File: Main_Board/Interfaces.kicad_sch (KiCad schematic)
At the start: 0 parts

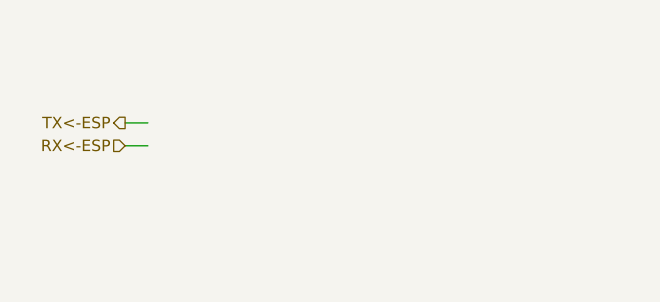
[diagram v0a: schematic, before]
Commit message: RS485 Transciever + Input Protection fix
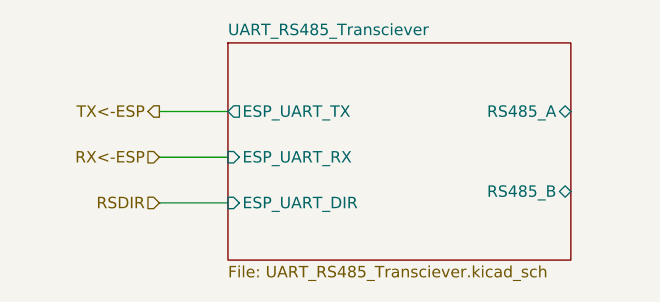
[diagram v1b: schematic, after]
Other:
- added sheet UART_RS485_Transciever (UART_RS485_Transciever.kicad_sch)
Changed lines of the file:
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@@
 	(wire
 		(pts
-			(xy 69.85 92.71) (xy 72.39 92.71)
+			(xy 73.66 91.44) (xy 81.28 91.44)
 		)
 		(stroke
@@
 	(wire
 		(pts
-			(xy 69.85 95.25) (xy 72.39 95.25)
+			(xy 73.66 101.6) (xy 81.28 101.6)
+		)
+		(stroke
+			(width 0)
+			(type default)
+		)
+	)
+	(wire
+		(pts
+			(xy 73.66 96.52) (xy 81.28 96.52)
 		)
 		(stroke
@@
 	(hierarchical_label "RX<-ESP"
 		(shape input)
-		(at 69.85 95.25 180)
+		(at 73.66 96.52 180)
+		(effects
+			(font
+				(size 1.27 1.27)
+			)
+			(justify right)
+		)
+	)
+	(hierarchical_label "RSDIR"
+		(shape input)
+		(at 73.66 101.6 180)
 		(effects
 			(font
@@
 	(hierarchical_label "TX<-ESP"
 		(shape output)
-		(at 69.85 92.71 180)
+		(at 73.66 91.44 180)
 		(effects
 			(font
@@
 		)
 	)
+	(sheet
+		(at 81.28 83.82)
+		(size 38.1 24.13)
+		(exclude_from_sim no)
+		(in_bom yes)
+		(on_board yes)
+		(dnp no)
+		(fields_autoplaced yes)
+		(stroke
+			(width 0.1524)
+			(type solid)
+		)
+		(fill
+			(color 0 0 0 0)
+		)
+		(property "Sheetname" "UART_RS485_Transciever"
+			(at 81.28 83.1084 0)
+			(show_name no)
+			(do_not_autoplace no)
+			(effects
+				(font
+					(size 1.27 1.27)
+				)
+				(justify left bottom)
+			)
+		)
+		(property "Sheetfile" "UART_RS485_Transciever.kicad_sch"
+			(at 81.28 108.5346 0)
+			(show_name no)
+			(do_not_autoplace no)
+			(effects
+				(font
+					(size 1.27 1.27)
+				)
+				(justify left top)
+			)
+		)
+		(pin "ESP_UART_DIR" input
+			(at 81.28 101.6 180)
+			(effects
+				(font
+					(size 1.27 1.27)
+				)
+				(justify left)
+			)
+		)
+		(pin "RS485_B" bidirectional
+			(at 119.38 100.33 0)
+			(effects
+				(font
+					(size 1.27 1.27)
+				)
+				(justify right)
+			)
+		)
+		(pin "ESP_UART_RX" input
+			(at 81.28 96.52 180)
+			(effects
+				(font
+					(size 1.27 1.27)
+				)
+				(justify left)
+			)
+		)
+		(pin "ESP_UART_TX" output
+			(at 81.28 91.44 180)
+			(effects
+				(font
+					(size 1.27 1.27)
+				)
+				(justify left)
+			)
+		)
+		(pin "RS485_A" bidirectional
+			(at 119.38 91.44 0)
+			(effects
+				(font
+					(size 1.27 1.27)
+				)
+				(justify right)
+			)
+		)
+		(instances
+			(project "Main_Board"
+				(path "/7481738f-7c20-40bb-99b0-6ccd4168db33/f339aa79-d1b1-4b60-b951-815db04e9281"
+					(page "9")
+				)
+			)
+		)
+	)

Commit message: Aesthetics/cleanup
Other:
- sheet UART_RS485_Transciever ports: added TRANSCIEVER_UART_DIR, TRANSCIEVER_UART_RX, TRANSCIEVER_UART_TX; removed ESP_UART_DIR, ESP_UART_RX, ESP_UART_TX
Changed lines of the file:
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@@
 	(wire
 		(pts
-			(xy 73.66 91.44) (xy 81.28 91.44)
+			(xy 73.66 101.6) (xy 81.28 101.6)
 		)
 		(stroke
@@
 	(wire
 		(pts
-			(xy 73.66 101.6) (xy 81.28 101.6)
+			(xy 73.66 91.44) (xy 81.28 91.44)
 		)
 		(stroke
@@
 		)
 	)
-	(hierarchical_label "RX<-ESP"
+	(hierarchical_label "MODULE_BUS_RX"
 		(shape input)
 		(at 73.66 96.52 180)
@@
 		)
 	)
-	(hierarchical_label "RSDIR"
+	(hierarchical_label "MODULE_BUS_DIR"
 		(shape input)
 		(at 73.66 101.6 180)
@@
 		)
 	)
-	(hierarchical_label "TX<-ESP"
+	(hierarchical_label "MODULE_BUS_TX"
 		(shape output)
 		(at 73.66 91.44 180)
@@
 			)
 		)
-		(pin "ESP_UART_DIR" input
-			(at 81.28 101.6 180)
-			(effects
-				(font
-					(size 1.27 1.27)
-				)
-				(justify left)
-			)
-		)
 		(pin "RS485_B" bidirectional
 			(at 119.38 100.33 0)
@@
 				)
 				(justify right)
-			)
-		)
-		(pin "ESP_UART_RX" input
-			(at 81.28 96.52 180)
-			(effects
-				(font
-					(size 1.27 1.27)
-				)
-				(justify left)
-			)
-		)
-		(pin "ESP_UART_TX" output
-			(at 81.28 91.44 180)
-			(effects
-				(font
-					(size 1.27 1.27)
-				)
-				(justify left)
 			)
 		)
@@
 			)
 		)
+		(pin "TRANSCIEVER_UART_DIR" input
+			(at 81.28 101.6 180)
+			(effects
+				(font
+					(size 1.27 1.27)
+				)
+				(justify left)
+			)
+		)
+		(pin "TRANSCIEVER_UART_RX" output
+			(at 81.28 96.52 180)
+			(effects
+				(font
+					(size 1.27 1.27)
+				)
+				(justify left)
+			)
+		)
+		(pin "TRANSCIEVER_UART_TX" input
+			(at 81.28 91.44 180)
+			(effects
+				(font
+					(size 1.27 1.27)
+				)
+				(justify left)
+			)
+		)

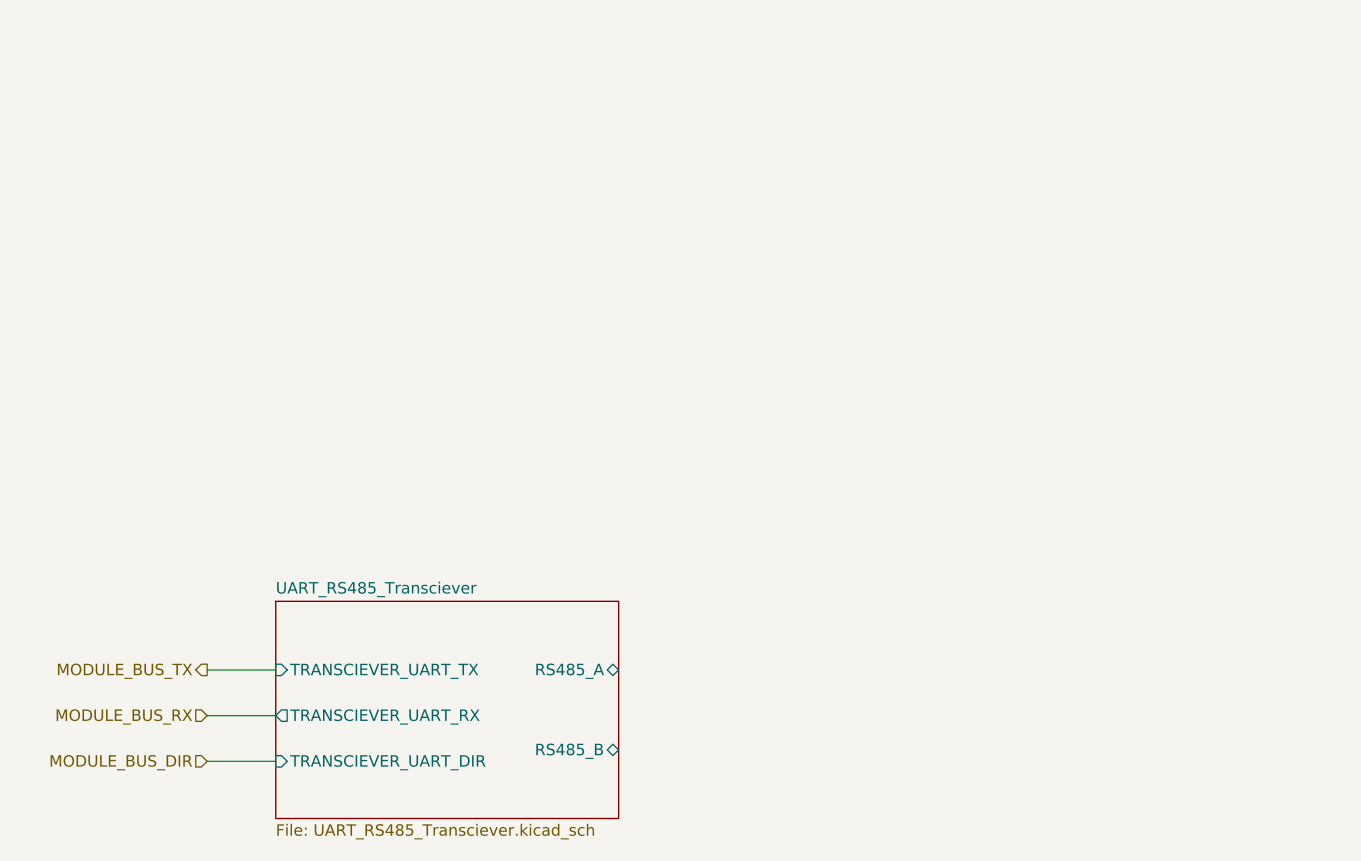
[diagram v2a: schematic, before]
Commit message: add external obrds interfaces
Todo pyro chanells
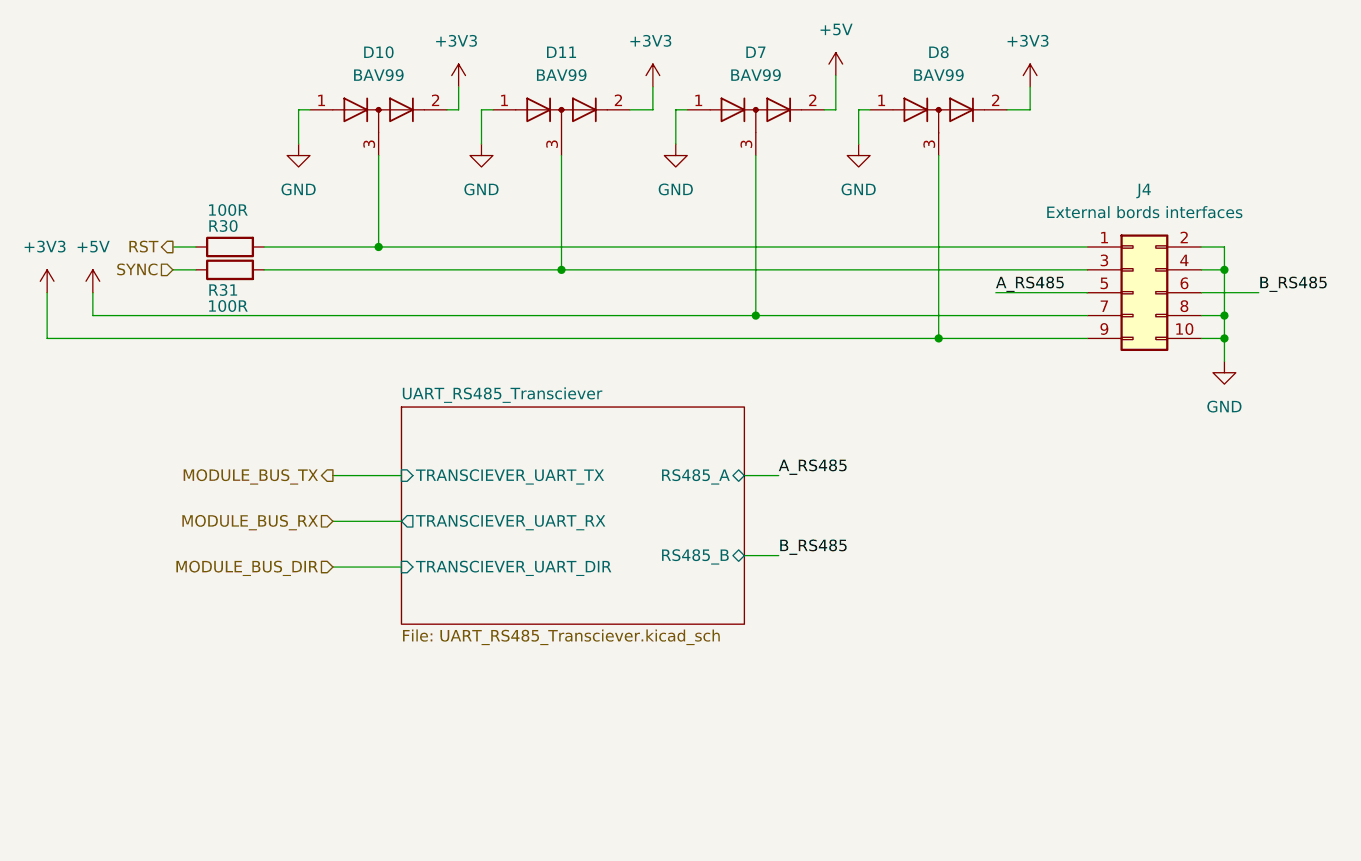
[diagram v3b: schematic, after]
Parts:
- added D10, D11, D7, D8: BAV99, Package_TO_SOT_SMD:SOT-23, symbol Diode:BAV99
- added J4: External bords interfaces, symbol Connector_Generic:Conn_02x05_Odd_Even
- added R30, R31: 100R, symbol Device:R
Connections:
- new net: D10.3 (K), J4.1 (Pin_1), R30.2
- new net: D11.3 (K), J4.3 (Pin_3), R31.2
- new net +3V3: D10.2 (A), D11.2 (A), D8.2 (A), D8.3 (K), J4.9 (Pin_9)
- new net +5V: D7.2 (A), D7.3 (K), J4.7 (Pin_7)
- new net A_RS485: J4.5 (Pin_5)
- new net B_RS485: J4.6 (Pin_6)
- new net GND: D10.1 (K), D11.1 (K), D7.1 (K), D8.1 (K), J4.10 (Pin_10), J4.2 (Pin_2), J4.4 (Pin_4), J4.8 (Pin_8)
- new net RST: R30.1
- new net SYNC: R31.1

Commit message: Add buzzer, Add LED, ADD R&D jumper
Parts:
- added BZ1: Buzzer, symbol Device:Buzzer
- added C27, C28, C29, C31: 10uF, symbol Device:C
- added C30, C32: 100nF, symbol Device:C
- added D11: WS2812B, LED_SMD:LED_WS2812B_PLCC4_5.0x5.0mm_P3.2mm, symbol LED:WS2812B
- added Q2: 2N7002, Package_TO_SOT_SMD:SOT-23, symbol Transistor_FET:2N7002
- added R28: 4k7, symbol Device:R
- renumbered D8 to D10, D10 to D7, D11 to D8, D7 to D9, R30 to R29, R31 to R30
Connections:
- net +5V: now also BZ1.1 (+), C27.1, C28.1, C29.1, C30.1, C31.1, C32.1, D11.1 (VDD)
- net GND: now also C27.2, C28.2, C29.2, C30.2, C31.2, C32.2, D11.3 (VSS), Q2.2 (S), R28.2
- new net: BZ1.2 (-), Q2.3 (D)
- new net BUZZER: Q2.1 (G), R28.1
- new net LED: D11.4 (DIN)
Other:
- note added: "TO_DO"
- moved on the sheet: D10, D7, D8, D9, J4, R29, R30

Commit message: ADD footprints
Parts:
- C27, C28, C29, C30, C31, C32: footprint (none) -> Capacitor_SMD:C_0603_1608Metric
- J4: footprint (none) -> Connector_PinHeader_1.27mm:PinHeader_2x05_P1.27mm_Horizontal
- R28, R29, R30: footprint (none) -> Resistor_SMD:R_0603_1608Metric
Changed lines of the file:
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@@
 			)
 		)
-		(property "Footprint" ""
+		(property "Footprint" "Capacitor_SMD:C_0603_1608Metric"
 			(at 186.3852 116.84 0)
 			(hide yes)
@@
 			)
 		)
-		(property "Footprint" ""
+		(property "Footprint" "Capacitor_SMD:C_0603_1608Metric"
 			(at 41.6052 163.83 0)
 			(hide yes)
@@
 			)
 		)
-		(property "Footprint" ""
+		(property "Footprint" "Resistor_SMD:R_0603_1608Metric"
 			(at 63.5 70.612 90)
 			(hide yes)
@@
 			)
 		)
-		(property "Footprint" ""
+		(property "Footprint" "Capacitor_SMD:C_0603_1608Metric"
 			(at 54.3052 163.83 0)
 			(hide yes)
@@
 			)
 		)
-		(property "Footprint" ""
+		(property "Footprint" "Capacitor_SMD:C_0603_1608Metric"
 			(at 199.0852 116.84 0)
 			(hide yes)
@@
 			)
 		)
-		(property "Footprint" ""
+		(property "Footprint" "Resistor_SMD:R_0603_1608Metric"
 			(at 55.372 181.61 90)
 			(hide yes)
@@
 			)
 		)
-		(property "Footprint" ""
+		(property "Footprint" "Capacitor_SMD:C_0603_1608Metric"
 			(at 30.1752 163.83 0)
 			(hide yes)
@@
 			)
 		)
-		(property "Footprint" ""
+		(property "Footprint" "Resistor_SMD:R_0603_1608Metric"
 			(at 63.5 76.708 90)
 			(hide yes)
@@
 			)
 		)
-		(property "Footprint" ""
+		(property "Footprint" "Connector_PinHeader_1.27mm:PinHeader_2x05_P1.27mm_Horizontal"
 			(at 163.83 77.47 0)
 			(hide yes)
@@
 			)
 		)
-		(property "Footprint" ""
+		(property "Footprint" "Capacitor_SMD:C_0603_1608Metric"
 			(at 18.7452 163.83 0)
 			(hide yes)

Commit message: PCB init
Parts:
- BZ1: footprint (none) -> Buzzer_Beeper:Buzzer_12x9.5RM7.6
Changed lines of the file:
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@@
 			)
 		)
-		(property "Footprint" ""
+		(property "Footprint" "Buzzer_Beeper:Buzzer_12x9.5RM7.6"
 			(at 70.485 153.67 90)
 			(hide yes)

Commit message: Add pyro channels x2
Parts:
- renumbered R28 to R30, R29 to R31, R30 to R32
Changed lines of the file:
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@@
 		(dnp no)
 		(fields_autoplaced yes)
-		(property "Reference" "#PWR078"
+		(property "Reference" "#PWR082"
 			(at 173.99 91.44 0)
 			(hide yes)
@@
 			(project "Main_Board"
 				(path "/7481738f-7c20-40bb-99b0-6ccd4168db33/f339aa79-d1b1-4b60-b951-815db04e9281"
-					(reference "#PWR078")
+					(reference "#PWR082")
 					(unit 1)
 				)
@@
 		(in_pos_files yes)
 		(dnp no)
-		(property "Reference" "R29"
+		(property "Reference" "R31"
 			(at 62.738 70.104 90)
 			(show_name no)
@@
 			(project "Main_Board"
 				(path "/7481738f-7c20-40bb-99b0-6ccd4168db33/f339aa79-d1b1-4b60-b951-815db04e9281"
-					(reference "R29")
+					(reference "R31")
 					(unit 1)
 				)
@@
 		(in_pos_files yes)
 		(dnp no)
-		(property "Reference" "#PWR065"
+		(property "Reference" "#PWR069"
 			(at 43.18 81.28 0)
 			(hide yes)
@@
 			(project "Main_Board"
 				(path "/7481738f-7c20-40bb-99b0-6ccd4168db33/f339aa79-d1b1-4b60-b951-815db04e9281"
-					(reference "#PWR065")
+					(reference "#PWR069")
 					(unit 1)
 				)
@@
 		(dnp no)
 		(fields_autoplaced yes)
-		(property "Reference" "#PWR064"
+		(property "Reference" "#PWR068"
 			(at 40.64 171.45 0)
 			(hide yes)
@@
 			(project "Main_Board"
 				(path "/7481738f-7c20-40bb-99b0-6ccd4168db33/f339aa79-d1b1-4b60-b951-815db04e9281"
-					(reference "#PWR064")
+					(reference "#PWR068")
 					(unit 1)
 				)
@@
 		(dnp no)
 		(fields_autoplaced yes)
-		(property "Reference" "#PWR068"
+		(property "Reference" "#PWR072"
 			(at 57.15 193.04 0)
 			(hide yes)
@@
 			(project "Main_Board"
 				(path "/7481738f-7c20-40bb-99b0-6ccd4168db33/f339aa79-d1b1-4b60-b951-815db04e9281"
-					(reference "#PWR068")
+					(reference "#PWR072")
 					(unit 1)
 				)
@@
 		(dnp no)
 		(fields_autoplaced yes)
-		(property "Reference" "#PWR067"
+		(property "Reference" "#PWR071"
 			(at 53.34 170.18 0)
 			(hide yes)
@@
 			(project "Main_Board"
 				(path "/7481738f-7c20-40bb-99b0-6ccd4168db33/f339aa79-d1b1-4b60-b951-815db04e9281"
-					(reference "#PWR067")
+					(reference "#PWR071")
 					(unit 1)
 				)
@@
 		(dnp no)
 		(fields_autoplaced yes)
-		(property "Reference" "R28"
+		(property "Reference" "R30"
 			(at 59.69 180.3399 0)
 			(show_name no)
@@
 			(project "Main_Board"
 				(path "/7481738f-7c20-40bb-99b0-6ccd4168db33/f339aa79-d1b1-4b60-b951-815db04e9281"
-					(reference "R28")
+					(reference "R30")
 					(unit 1)
 				)
@@
 		(dnp no)
 		(fields_autoplaced yes)
-		(property "Reference" "#PWR076"
+		(property "Reference" "#PWR080"
 			(at 133.35 67.31 0)
 			(hide yes)
@@
 			(project "Main_Board"
 				(path "/7481738f-7c20-40bb-99b0-6ccd4168db33/f339aa79-d1b1-4b60-b951-815db04e9281"
-					(reference "#PWR076")
+					(reference "#PWR080")
 					(unit 1)
 				)
@@
 		(dnp no)
 		(fields_autoplaced yes)
-		(property "Reference" "#PWR062"
+		(property "Reference" "#PWR066"
 			(at 17.78 171.45 0)
 			(hide yes)
@@
 			(project "Main_Board"
 				(path "/7481738f-7c20-40bb-99b0-6ccd4168db33/f339aa79-d1b1-4b60-b951-815db04e9281"
-					(reference "#PWR062")
+					(reference "#PWR066")
 					(unit 1)
 				)
@@
 		(dnp no)
 		(fields_autoplaced yes)
-		(property "Reference" "#PWR075"
+		(property "Reference" "#PWR079"
 			(at 130.81 57.15 0)
 			(hide yes)
@@
 			(project "Main_Board"
 				(path "/7481738f-7c20-40bb-99b0-6ccd4168db33/f339aa79-d1b1-4b60-b951-815db04e9281"
-					(reference "#PWR075")
+					(reference "#PWR079")
 					(unit 1)
 				)
@@
 		(dnp no)
 		(fields_autoplaced yes)
-		(property "Reference" "#PWR082"
+		(property "Reference" "#PWR086"
 			(at 222.25 134.62 0)
 			(hide yes)
@@
 			(project "Main_Board"
 				(path "/7481738f-7c20-40bb-99b0-6ccd4168db33/f339aa79-d1b1-4b60-b951-815db04e9281"
-					(reference "#PWR082")
+					(reference "#PWR086")
 					(unit 1)
 				)
@@
 		(dnp no)
 		(fields_autoplaced yes)
-		(property "Reference" "#PWR074"
+		(property "Reference" "#PWR078"
 			(at 113.03 67.31 0)
 			(hide yes)
@@
 			(project "Main_Board"
 				(path "/7481738f-7c20-40bb-99b0-6ccd4168db33/f339aa79-d1b1-4b60-b951-815db04e9281"
-					(reference "#PWR074")
+					(reference "#PWR078")
 					(unit 1)
 				)
@@
 		(dnp no)
 		(fields_autoplaced yes)
-		(property "Reference" "#PWR081"
+		(property "Reference" "#PWR085"
 			(at 222.25 109.22 0)
 			(hide yes)
@@
 			(project "Main_Board"
 				(path "/7481738f-7c20-40bb-99b0-6ccd4168db33/f339aa79-d1b1-4b60-b951-815db04e9281"
-					(reference "#PWR081")
+					(reference "#PWR085")
 					(unit 1)
 				)
@@
 		(dnp no)
 		(fields_autoplaced yes)
-		(property "Reference" "#PWR070"
+		(property "Reference" "#PWR074"
 			(at 71.12 67.31 0)
 			(hide yes)
@@
 			(project "Main_Board"
 				(path "/7481738f-7c20-40bb-99b0-6ccd4168db33/f339aa79-d1b1-4b60-b951-815db04e9281"
-					(reference "#PWR070")
+					(reference "#PWR074")
 					(unit 1)
 				)
@@
 		(in_pos_files yes)
 		(dnp no)
-		(property "Reference" "R30"
+		(property "Reference" "R32"
 			(at 62.738 77.216 90)
 			(show_name no)
@@
 			(project "Main_Board"
 				(path "/7481738f-7c20-40bb-99b0-6ccd4168db33/f339aa79-d1b1-4b60-b951-815db04e9281"
-					(reference "R30")
+					(reference "R32")
 					(unit 1)
 				)
@@
 		(dnp no)
 		(fields_autoplaced yes)
-		(property "Reference" "#PWR061"
+		(property "Reference" "#PWR065"
 			(at 17.78 156.21 0)
 			(hide yes)
@@
 			(project "Main_Board"
 				(path "/7481738f-7c20-40bb-99b0-6ccd4168db33/f339aa79-d1b1-4b60-b951-815db04e9281"
-					(reference "#PWR061")
+					(reference "#PWR065")
 					(unit 1)
 				)
@@
 		(in_pos_files yes)
 		(dnp no)
-		(property "Reference" "#PWR073"
+		(property "Reference" "#PWR077"
 			(at 110.49 58.42 0)
 			(hide yes)
@@
 			(project "Main_Board"
 				(path "/7481738f-7c20-40bb-99b0-6ccd4168db33/f339aa79-d1b1-4b60-b951-815db04e9281"
-					(reference "#PWR073")
+					(reference "#PWR077")
 					(unit 1)
 				)
@@
 		(dnp no)
 		(fields_autoplaced yes)
-		(property "Reference" "#PWR069"
+		(property "Reference" "#PWR073"
 			(at 68.58 193.04 0)
 			(hide yes)
@@
 			(project "Main_Board"
 				(path "/7481738f-7c20-40bb-99b0-6ccd4168db33/f339aa79-d1b1-4b60-b951-815db04e9281"
-					(reference "#PWR069")
+					(reference "#PWR073")
 					(unit 1)
 				)
@@
 		(dnp no)
 		(fields_autoplaced yes)
-		(property "Reference" "#PWR080"
+		(property "Reference" "#PWR084"
 			(at 198.12 125.73 0)
 			(hide yes)
@@
 			(project "Main_Board"
 				(path "/7481738f-7c20-40bb-99b0-6ccd4168db33/f339aa79-d1b1-4b60-b951-815db04e9281"
-					(reference "#PWR080")
+					(reference "#PWR084")
 					(unit 1)
 				)
@@
 		(dnp no)
 		(fields_autoplaced yes)
-		(property "Reference" "#PWR079"
+		(property "Reference" "#PWR083"
 			(at 185.42 124.46 0)
 			(hide yes)
@@
 			(project "Main_Board"
 				(path "/7481738f-7c20-40bb-99b0-6ccd4168db33/f339aa79-d1b1-4b60-b951-815db04e9281"
-					(reference "#PWR079")
+					(reference "#PWR083")
 					(unit 1)
 				)
@@
 		(dnp no)
 		(fields_autoplaced yes)
-		(property "Reference" "#PWR063"
+		(property "Reference" "#PWR067"
 			(at 29.21 171.45 0)
 			(hide yes)
@@
 			(project "Main_Board"
 				(path "/7481738f-7c20-40bb-99b0-6ccd4168db33/f339aa79-d1b1-4b60-b951-815db04e9281"
-					(reference "#PWR063")
+					(reference "#PWR067")
 					(unit 1)
 				)
@@
 		(in_pos_files yes)
 		(dnp no)
-		(property "Reference" "#PWR077"
+		(property "Reference" "#PWR081"
 			(at 152.4 58.42 0)
 			(hide yes)
@@
 			(project "Main_Board"
 				(path "/7481738f-7c20-40bb-99b0-6ccd4168db33/f339aa79-d1b1-4b60-b951-815db04e9281"
-					(reference "#PWR077")
+					(reference "#PWR081")
 					(unit 1)
 				)
@@
 		(dnp no)
 		(fields_autoplaced yes)
-		(property "Reference" "#PWR066"
+		(property "Reference" "#PWR070"
 			(at 48.26 81.28 0)
 			(hide yes)
@@
 			(project "Main_Board"
 				(path "/7481738f-7c20-40bb-99b0-6ccd4168db33/f339aa79-d1b1-4b60-b951-815db04e9281"
-					(reference "#PWR066")
+					(reference "#PWR070")
 					(unit 1)
 				)
@@
 		(dnp no)
 		(fields_autoplaced yes)
-		(property "Reference" "#PWR072"
+		(property "Reference" "#PWR076"
 			(at 91.44 67.31 0)
 			(hide yes)
@@
 			(project "Main_Board"
 				(path "/7481738f-7c20-40bb-99b0-6ccd4168db33/f339aa79-d1b1-4b60-b951-815db04e9281"
-					(reference "#PWR072")
+					(reference "#PWR076")
 					(unit 1)
 				)
@@
 		(in_pos_files yes)
 		(dnp no)
-		(property "Reference" "#PWR071"
+		(property "Reference" "#PWR075"
 			(at 88.9 58.42 0)
 			(hide yes)
@@
 			(project "Main_Board"
 				(path "/7481738f-7c20-40bb-99b0-6ccd4168db33/f339aa79-d1b1-4b60-b951-815db04e9281"
-					(reference "#PWR071")
-					(unit 1)
-				)
+					(reference "#PWR075")
+					(unit 1)
+				)
